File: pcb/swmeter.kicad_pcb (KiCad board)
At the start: 2 copper layers, 79.6 x 70 mm, 34 parts, among them J1 AudioPlug, J2 Conn_Coaxial, J3 Conn_01x03_Female, SW1 SW_SPDT, SW2 SW_SPDT, SW3 SW_DIP_x02, U1 LM3914N

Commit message: update v0.4
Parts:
- removed BT1: Battery_Cell, Battery:BatteryHolder_Eagle_12BH611-GR
- removed CV1: 22µF, Capacitor_THT:CP_Radial_D5.0mm_P2.50mm
- added C1: 22µF, Capacitor_THT:CP_Radial_D5.0mm_P2.50mm, F.Cu at (257.4, 126.3)
- added G1: LOGO, TheBrutzlers_Lib:approved_theBrutzler, F.Cu at (219.7, 122.5)
- added G11: LOGO, TheBrutzlers_Lib:approved_theBrutzler, B.Cu at (219.4, 122.5)
- added J0: Conn_01x02_Female, Connector_PinHeader_2.54mm:PinHeader_1x02_P2.54mm_Vertical, F.Cu at (210.0, 96.7)
- moved REF4 145.6 mm to (231.1, 137.1)
- moved REF44 145.3 mm to (230.8, 137.0)
- moved R1 117.4 mm to (259.3, 117.4), turned to 180 degrees
- moved REF3 108.6 mm to (207.4, 122.3)
- moved REF33 108.5 mm to (207.3, 122.3)
- moved SW3 107.6 mm to (237.2, 106.1), turned to -90 degrees
- moved RV2 107.5 mm to (251.6, 111.3)
- moved D2 104.0 mm to (253.3, 145.5), turned to -90 degrees
- moved SW2 103.8 mm to (247.9, 91.3)
- moved U1 102.4 mm to (252.5, 123.4), turned to -90 degrees
- moved J3 101.6 mm to (250.0, 105.9), turned to -90 degrees
- moved RV1 98.5 mm to (241.3, 111.2)
- moved D3 97.5 mm to (248.7, 145.5), turned to -90 degrees
- moved D0 95.3 mm to (243.9, 107.3), turned to 90 degrees
- moved D4 91.2 mm to (244.1, 145.5), turned to -90 degrees
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- renumbered D2 to D10, D10 to D2, D9 to D3, D8 to D4, D7 to D5, D5 to D7, D4 to D8, D3 to D9
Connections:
- SW3 pad 2: Net-(D0-Pad1) -> Net-(RV1-Pad1)
- SW3 pad 3: Net-(RV1-Pad1) -> GND
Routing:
- net GND: track 131.8 -> 0.59 mm, vias 33 -> 118
- net Net-(C1-Pad1): track 119.8 -> 175.7 mm
- net Net-(SW3-Pad4): track 50.0 -> 11.7 mm
- net Net-(D0-Pad1): track 36.5 -> 3.95 mm
- net Net-(J1-PadR): track 49.7 -> 20.6 mm
- net Net-(D0-Pad2): track 24.0 -> 8.28 mm
- net Net-(R1-Pad2): track 16.9 -> 32.3 mm
- net Net-(D1-Pad1): track 46.2 -> 34.3 mm
- net Net-(RV2-Pad2): track 12.8 -> 23.9 mm
- net Net-(D5-Pad1): track 7.41 -> 16.7 mm
- net Net-(D6-Pad1): track 8.30 -> 17.6 mm
- net Net-(D4-Pad1): track 6.66 -> 15.9 mm
- net Net-(D3-Pad1): track 5.91 -> 15.1 mm
- net Net-(RV2-Pad1): track 15.0 -> 23.7 mm
- net Net-(J2-Pad1): track 21.6 -> 13.2 mm
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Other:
- board size 79.6 x 70 mm -> 60 x 66 mm
- board text added: "+9V"
- board text added: "-GND"
- board text added: "C1"
- board text added: "DC_Met."
- board text added: "J0"
- board text added: "R<>Ext."
- board text added: "RF<>Ext."
- board text added: "SW-Meter v0.3 by WodoWiesel ©26/11/2022"
- board text added: "SW-Meter v0.4 by WodoWiesel ©08/12/2022"
- board text added: "ext.M_in"
- board text removed: "+/9V"
- board text removed: "-/GND"
- board text removed: "Battery"
- board text removed: "CV1"
- board text removed: "DC- Meter"
- board text removed: "R<->Ext."
- board text removed: "RF<->Ext."
- board text removed: "SW-Meter v0.2 by WodoWiesel © 20/10/2022"
- board text removed: "approved by theBrutzeler"
- board text removed: "extern Meter_in"

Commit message: make pretty
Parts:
- moved REF44 1.61 mm to (231.0, 138.6)
- moved U1 1.48 mm to (252.5, 124.9)
- moved REF4 1.48 mm to (231.1, 138.6)
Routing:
- net Net-(R1-Pad2): track 32.3 -> 34.9 mm
- net GND: track 0.59 -> 3.25 mm, vias 118 -> 127
- net Net-(RV2-Pad1): track 23.7 -> 26.0 mm
- net Net-(C1-Pad1): track 175.7 -> 177.9 mm
- net Net-(J3-Pad2): track 20.2 -> 21.7 mm
- net Net-(SW3-Pad4): track 11.7 -> 13.2 mm
- net Net-(D4-Pad1): track 15.9 -> 14.4 mm
- net Net-(D7-Pad1): track 18.5 -> 17.0 mm
- net Net-(D6-Pad1): track 17.6 -> 16.1 mm
- net Net-(D3-Pad1): track 15.1 -> 13.6 mm
- net Net-(D2-Pad1): track 14.8 -> 13.4 mm
- net Net-(D5-Pad1): track 16.7 -> 15.3 mm
- net Net-(RV2-Pad2): track 23.9 -> 25.3 mm
- net Net-(D8-Pad1): track 19.3 -> 17.9 mm
- net Net-(D1-Pad1): track 34.3 -> 34.9 mm
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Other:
- board text added: "ADJ REF"
- board text added: "ADJ REV"
- board text added: "DC_Meter"
- board text added: "SW-Meter v0.4 by WodoWiesel ©17/12/2022"
- board text removed: "ADJ"
- board text removed: "DC_Met."
- board text removed: "R<>Ext."
- board text removed: "SW-Meter v0.3 by WodoWiesel ©26/11/2022"
- board text removed: "SW-Meter v0.4 by WodoWiesel ©08/12/2022"

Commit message: improve readability
improve readability
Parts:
- moved G11 3.56 mm to (222.8, 123.6), turned to -90 degrees
- moved G1 3.49 mm to (222.9, 123.7), turned to 90 degrees
- moved J0 0.25 mm to (209.9, 96.9)
- moved SW3 0.25 mm to (237.0, 106.3)
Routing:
- net Net-(RV1-Pad1): track 9.97 -> 10.7 mm
- net GND: track 3.25 -> 2.97 mm, vias 127 -> 129
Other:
- board text added: "REF"
- board text added: "RF<|>ext."
- board text added: "SW-Meter v0.4 © WodoWiesel 05/03/2023"
- board text removed: "ADJ REF"
- board text removed: "ADJ REV"
- board text removed: "RF<>Ext."
- board text removed: "SW-Meter v0.4 by WodoWiesel ©17/12/2022"

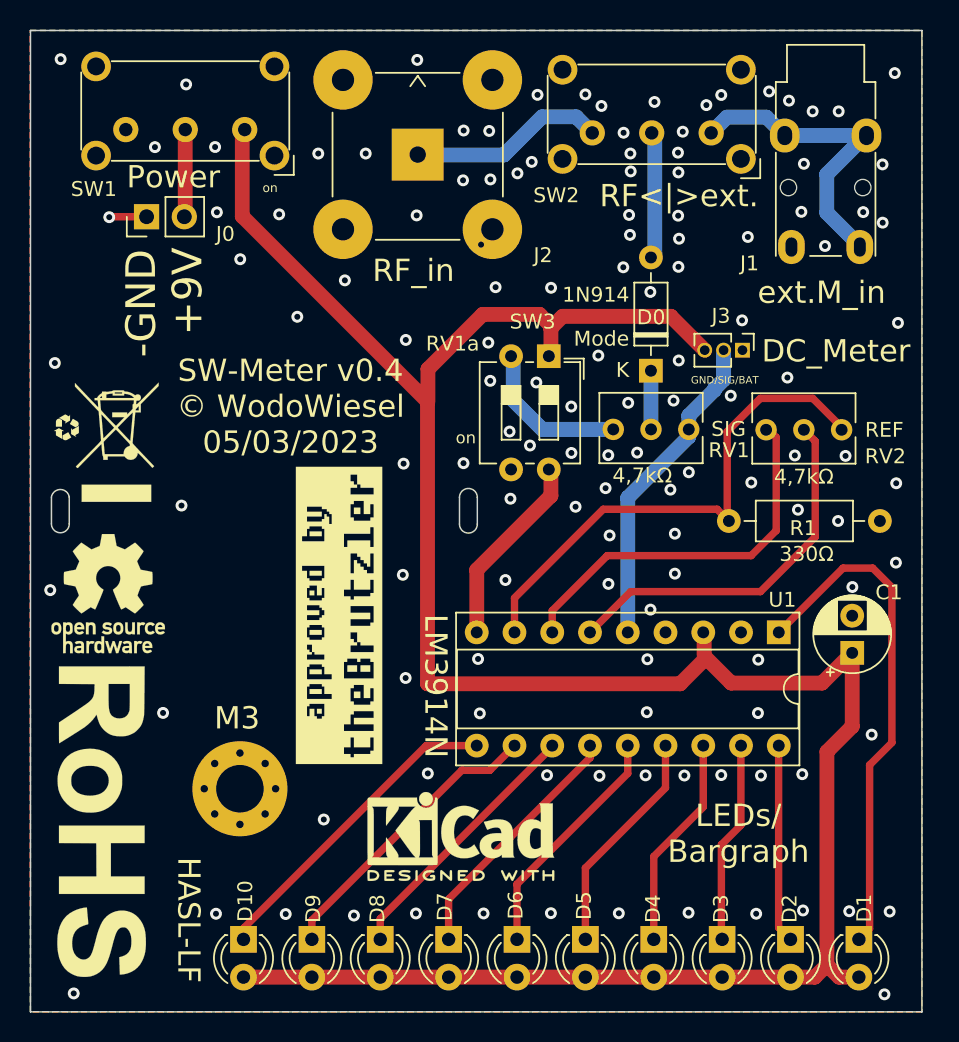
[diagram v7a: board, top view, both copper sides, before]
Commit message: -update to compact bargraph design -add capacitor for battery
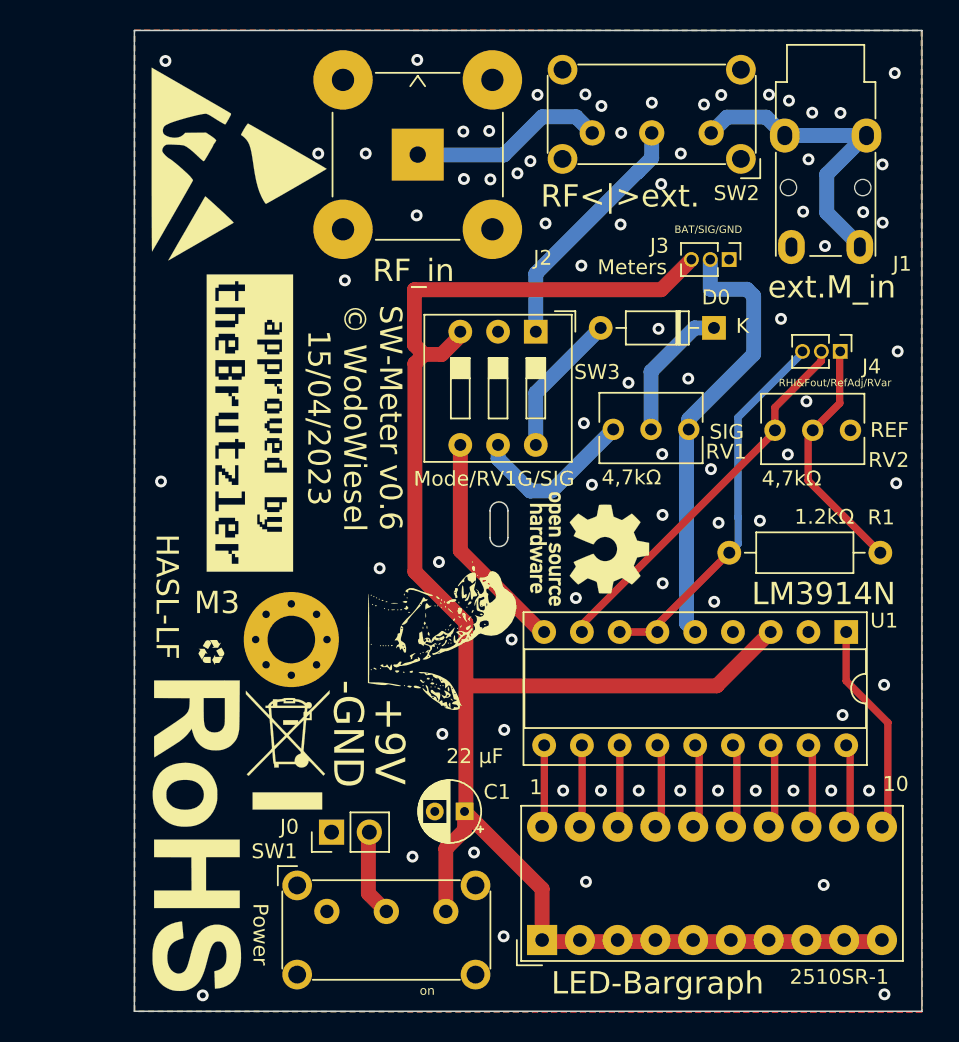
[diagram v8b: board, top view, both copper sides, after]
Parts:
- removed D1, D10, D3, D4, D5, D6, D7, D8, D9: LED, LED_THT:LED_D3.0mm_Clear
- removed D2: red, LED_THT:LED_D3.0mm_Clear
- removed REF4, REF44: KiCad-Logo2_5mm_SilkScreen, Symbol:KiCad-Logo2_5mm_SilkScreen
- added BAR1: 2510SR-1, Display:HDSP-4836, F.Cu at (236.6, 145.6)
- added G2: LOGO, Logos:wiesel-kicad-back-white, F.Cu at (229.8, 125.1)
- added G22: LOGO, Logos:wiesel-kicad-back-white, B.Cu at (229.8, 125.4)
- added J4: Conn_01x03_Female, Connector_PinHeader_1.27mm:PinHeader_1x03_P1.27mm_Vertical, F.Cu at (256.6, 106.0)
- added REF**: ESD-Logo_13.2x12mm_SilkScreen, Symbol:ESD-Logo_13.2x12mm_SilkScreen, F.Cu at (216.2, 93.4)
- C1: value 22µF -> 22 µF; footprint Capacitor_THT:CP_Radial_D5.0mm_P2.50mm -> Capacitor_THT:CP_Radial_D4.0mm_P2.00mm
- D0: value 1N914 -> 1N5711
- R1: value 330Ω -> 1.2kΩ
- SW3: value SW_DIP_x02 -> SW_DIP_x03; footprint Button_Switch_THT:SW_DIP_SPSTx02_Slide_6.7x6.64mm_W7.62mm_P2.54mm_LowProfile -> Button_Switch_THT:SW_DIP_SPSTx03_Slide_9.78x9.8mm_W7.62mm_P2.54mm
- moved SW1 52.9 mm to (222.1, 143.7), turned to 0 degrees
- moved J0 43.2 mm to (222.4, 138.3)
- moved REF33 32.6 mm to (239.8, 119.3), turned to 90 degrees
- moved REF3 32.5 mm to (239.8, 119.3), turned to -90 degrees
- moved C1 28.2 mm to (231.3, 136.9), turned to 180 degrees
- moved REF00 23.7 mm to (219.4, 132.7)
- moved REF0 23.7 mm to (219.4, 132.8)
- moved G9 18.0 mm to (214.3, 126.2), turned to 0 degrees
- moved G99 17.9 mm to (214.4, 126.1), turned to 180 degrees
- moved G1 14.3 mm to (216.9, 110.8), turned to -90 degrees
- moved G11 13.9 mm to (217.0, 111.0), turned to 90 degrees
- moved REF1 10.6 mm to (219.7, 125.4)
- moved REF55 7.07 mm to (213.5, 138.3)
- moved REF5 6.47 mm to (213.3, 138.6)
- moved J3 6.16 mm to (249.1, 99.8)
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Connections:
- C1 pad 1: Net-(C1-Pad1) -> Net-(BAR1-Pad1)
- J3 pad 3: Net-(C1-Pad1) -> Net-(BAR1-Pad1)
- R1 pad 1: GND -> Net-(J4-Pad1)
- R1 pad 2: Net-(R1-Pad2) -> Net-(J4-Pad3)
- RV2 pad 1: Net-(RV2-Pad1) -> Net-(J4-Pad2)
- RV2 pad 2: Net-(RV2-Pad2) -> Net-(J4-Pad1)
- RV2 pad 3: Net-(R1-Pad2) -> GND
- SW1 pad 1: Net-(C1-Pad1) -> unconnected-(SW1-Pad1)
- SW1 pad 3: unconnected-(SW1-Pad3) -> Net-(BAR1-Pad1)
- SW2 pad 2: Net-(D0-Pad2) -> Net-(SW2-Pad2)
- SW3 pad 1: Net-(C1-Pad1) -> Net-(SW2-Pad2)
- SW3 pad 2: Net-(RV1-Pad1) -> GND
- SW3 pad 3: GND -> Net-(BAR1-Pad1)
- U1 pad 3: Net-(C1-Pad1) -> Net-(BAR1-Pad1)
- U1 pad 6: Net-(RV2-Pad2) -> Net-(J4-Pad3)
- U1 pad 7: Net-(RV2-Pad1) -> Net-(J4-Pad3)
- U1 pad 8: Net-(R1-Pad2) -> Net-(J4-Pad2)
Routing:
- net Net-(C1-Pad1): track 177.9 -> 0.00 mm
- net Net-(BAR1-Pad1): track 0.00 -> 122.4 mm
- net Net-(R1-Pad2): track 35.0 -> 0.00 mm
- net Net-(RV2-Pad1): track 26.0 -> 0.00 mm
- net Net-(J4-Pad2): track 0.00 -> 25.5 mm
- net Net-(RV2-Pad2): track 25.3 -> 0.00 mm
- net Net-(J4-Pad3): track 0.00 -> 25.2 mm
- net Net-(BAR1-Pad11): track 34.5 -> 14.4 mm
- net Net-(SW2-Pad2): track 0.00 -> 16.6 mm
- net Net-(J4-Pad1): track 0.00 -> 16.4 mm
- net Net-(BAR1-Pad20): track 21.5 -> 5.38 mm
- net Net-(BAR1-Pad19): track 19.8 -> 5.59 mm
- net Net-(BAR1-Pad18): track 17.8 -> 5.59 mm
- net Net-(BAR1-Pad17): track 17.0 -> 6.01 mm
- net Net-(BAR1-Pad16): track 16.1 -> 5.76 mm
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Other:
- board size 60 x 66 mm -> 53 x 66 mm
- board text added: "1"
- board text added: "1.2kΩ"
- board text added: "10"
- board text added: "1N5711"
- board text added: "2510SR-1"
- board text added: "BAT/SIG/GND"
- board text added: "J4"
- board text added: "LED-Bargraph"
- board text added: "Meters"
- board text added: "Mode/RV1G/SIG"
- board text added: "RHI&Fout/RefAdj/RVar"
- board text added: "RVar/RefAdj/RHI&Fout"
- board text added: "SIG/RV1G/Mode"
- board text added: "SW-Meter v0.6 © WodoWiesel 15/04/2023"
- board text removed: "1N914"
- board text removed: "330Ω"
- board text removed: "D1"
- board text removed: "D10"
- board text removed: "D2"
- board text removed: "D3"
- board text removed: "D4"
- board text removed: "D5"
- board text removed: "D6"
- board text removed: "D7"
- board text removed: "D8"
- board text removed: "D9"
- board text removed: "DC_Meter"
- board text removed: "K"
- board text removed: "LEDs/ Bargraph"
- board text removed: "Mode"
- board text removed: "RV1a"
- board text removed: "SW-Meter v0.4 © WodoWiesel 05/03/2023"
